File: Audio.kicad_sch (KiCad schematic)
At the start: 9 parts, among them J2 Speaker, U1 MAX98357A/B, U4 CD4051B

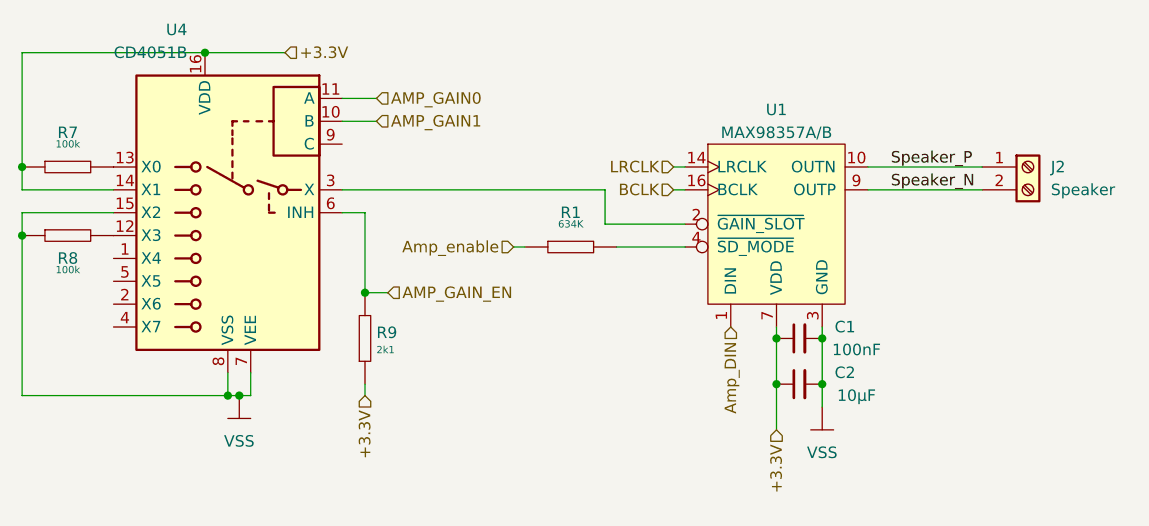
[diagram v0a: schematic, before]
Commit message: Améliorations après retour Victor
Allumage du régulateur maintenant géré par la teensy
Compaction de la carte pour rentrer sur 100x100mm
Ajout des trous de montage
Routage de la puissance du port USB maintenant sans boucle !
Un peu plus d'espace pour l'ampli'
Routage de l'ampli' avec des plans sur la sortie et une via par
condo pour l'entrée.
Moins de vias thermiques
Un seule via dans le pad de l'ampli'
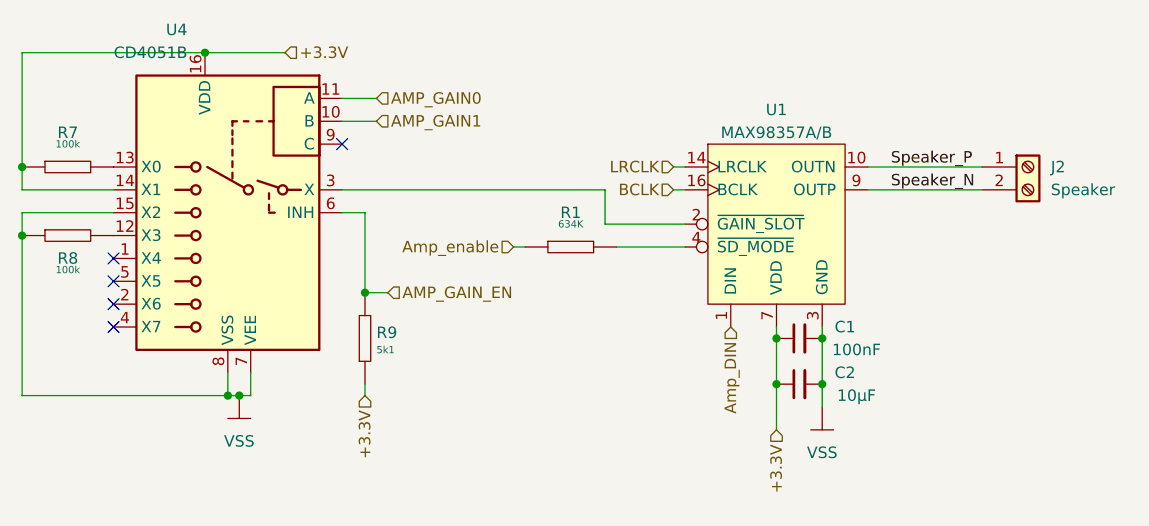
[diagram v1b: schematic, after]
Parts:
- R9: value RES_0603_2K1_1% -> RES_0603_5K1_1%; Resistance 2k1 -> 5k1
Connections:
- no-connect marks 0 -> 5
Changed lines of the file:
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@@
   (title_block
     (title "Projet Barbapapa")
-    (date "2023-06-19")
-    (rev "0.1")
+    (date "2023-06-22")
+    (rev "0.2")
     (company "Téo-CD")
   )
@@
   (junction (at 111.76 72.39) (diameter 0) (color 0 0 0 0)
   )
+  (no_connect (at 33.02 71.12))
+  (no_connect (at 58.42 50.8))
+  (no_connect (at 33.02 68.58))
+  (no_connect (at 33.02 63.5))
+  (no_connect (at 33.02 66.04))
   (wire (pts (xy 78.74 62.23) (xy 77.47 62.23))
     (stroke (width 0) (type default))
@@
     (pin "2")
     (instances
-      (project "Projet_JIN"
+      (project "Projet_Barbapapa"
         (path "/1f7900b2-90c4-494b-ac10-3ced4db03c46"
           (reference "J2") (unit 1)
@@
     (pin "VSS")
     (instances
-      (project "Projet_JIN"
+      (project "Projet_Barbapapa"
         (path "/1f7900b2-90c4-494b-ac10-3ced4db03c46/6cd5a50a-ff0a-4158-bf93-a56892953603"
           (reference "#VSS0101") (unit 1)
@@
     (pin "9")
     (instances
-      (project "Projet_JIN"
+      (project "Projet_Barbapapa"
         (path "/1f7900b2-90c4-494b-ac10-3ced4db03c46/6cd5a50a-ff0a-4158-bf93-a56892953603"
           (reference "U4") (unit 1)
@@
     (pin "2")
     (instances
-      (project "Projet_JIN"
+      (project "Projet_Barbapapa"
         (path "/1f7900b2-90c4-494b-ac10-3ced4db03c46/6cd5a50a-ff0a-4158-bf93-a56892953603"
           (reference "R7") (unit 1)
@@
     (pin "2")
     (instances
-      (project "Projet_JIN"
+      (project "Projet_Barbapapa"
         (path "/1f7900b2-90c4-494b-ac10-3ced4db03c46/6cd5a50a-ff0a-4158-bf93-a56892953603"
           (reference "R8") (unit 1)
@@
     (pin "2")
     (instances
-      (project "Projet_JIN"
+      (project "Projet_Barbapapa"
         (path "/1f7900b2-90c4-494b-ac10-3ced4db03c46/6cd5a50a-ff0a-4158-bf93-a56892953603"
           (reference "R1") (unit 1)
@@
       (effects (font (size 1.27 1.27)) (justify right))
     )
-    (property "Value" "RES_0603_2K1_1%" (at 53.34 68.58 0)
+    (property "Value" "RES_0603_5K1_1%" (at 53.34 68.58 0)
       (effects (font (size 1.27 1.27)) hide)
     )
@@
       (effects (font (size 1.27 1.27)) hide)
     )
-    (property "Resistance" "2k1" (at 62.23 73.66 90)
+    (property "Resistance" "5k1" (at 62.23 73.66 90)
       (effects (font (size 0.8 0.8)) (justify right))
     )
@@
     (pin "2")
     (instances
-      (project "Projet_JIN"
+      (project "Projet_Barbapapa"
         (path "/1f7900b2-90c4-494b-ac10-3ced4db03c46/6cd5a50a-ff0a-4158-bf93-a56892953603"
           (reference "R9") (unit 1)
@@
     (pin "2")
     (instances
-      (project "Projet_JIN"
+      (project "Projet_Barbapapa"
         (path "/1f7900b2-90c4-494b-ac10-3ced4db03c46/6cd5a50a-ff0a-4158-bf93-a56892953603"
           (reference "C1") (unit 1)
@@
     (pin "VSS")
     (instances
-      (project "Projet_JIN"
+      (project "Projet_Barbapapa"
         (path "/1f7900b2-90c4-494b-ac10-3ced4db03c46/6cd5a50a-ff0a-4158-bf93-a56892953603"
           (reference "#VSS010") (unit 1)
@@
     (pin "2")
     (instances
-      (project "Projet_JIN"
+      (project "Projet_Barbapapa"
         (path "/1f7900b2-90c4-494b-ac10-3ced4db03c46/6cd5a50a-ff0a-4158-bf93-a56892953603"
           (reference "C2") (unit 1)
@@
     (pin "9")
     (instances
-      (project "Projet_JIN"
+      (project "Projet_Barbapapa"
         (path "/1f7900b2-90c4-494b-ac10-3ced4db03c46/6cd5a50a-ff0a-4158-bf93-a56892953603"
           (reference "U1") (unit 1)

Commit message: Rev 0.3: Passage sur deux couches
Passage sur deux couches, ajustement de l'impédance pour l'USB.
Reroutage de l'alimentation côté USB
Ajout de beaucoup de silk
Quelques ajustements de nets pour la lisbilité
Ajout de LEDs de debug
Plan de masse sur le top
Quelques mises à jour sur le schematic
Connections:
- net +3.3V is gone; now on net VDD: C1.1, C2.1, R7.1, R9.1, U1.7 (VDD), U4.14 (X1), U4.16 (VDD)
- net VSS is gone; now on net GND: C1.2, C2.2, R8.1, U1.3 (GND), U4.15 (X2), U4.7 (VEE), U4.8 (VSS)
- net GND: now also U1.17 (GND)
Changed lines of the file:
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@@
   (title_block
     (title "Projet Barbapapa")
-    (date "2023-06-22")
-    (rev "0.2")
+    (date "2023-06-25")
+    (rev "0.3")
     (company "Téo-CD")
   )
@@
     (pin "11")
     (pin "15")
+    (pin "17")
     (pin "2")
     (pin "3")
